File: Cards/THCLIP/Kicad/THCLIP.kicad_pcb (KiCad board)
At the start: 2 copper layers, 47.3 x 35.4 mm, 11 parts, among them J2 Conn_01x03_Pin, J3 Conn_01x05_Pin, U1 RS3K-2424S/H3

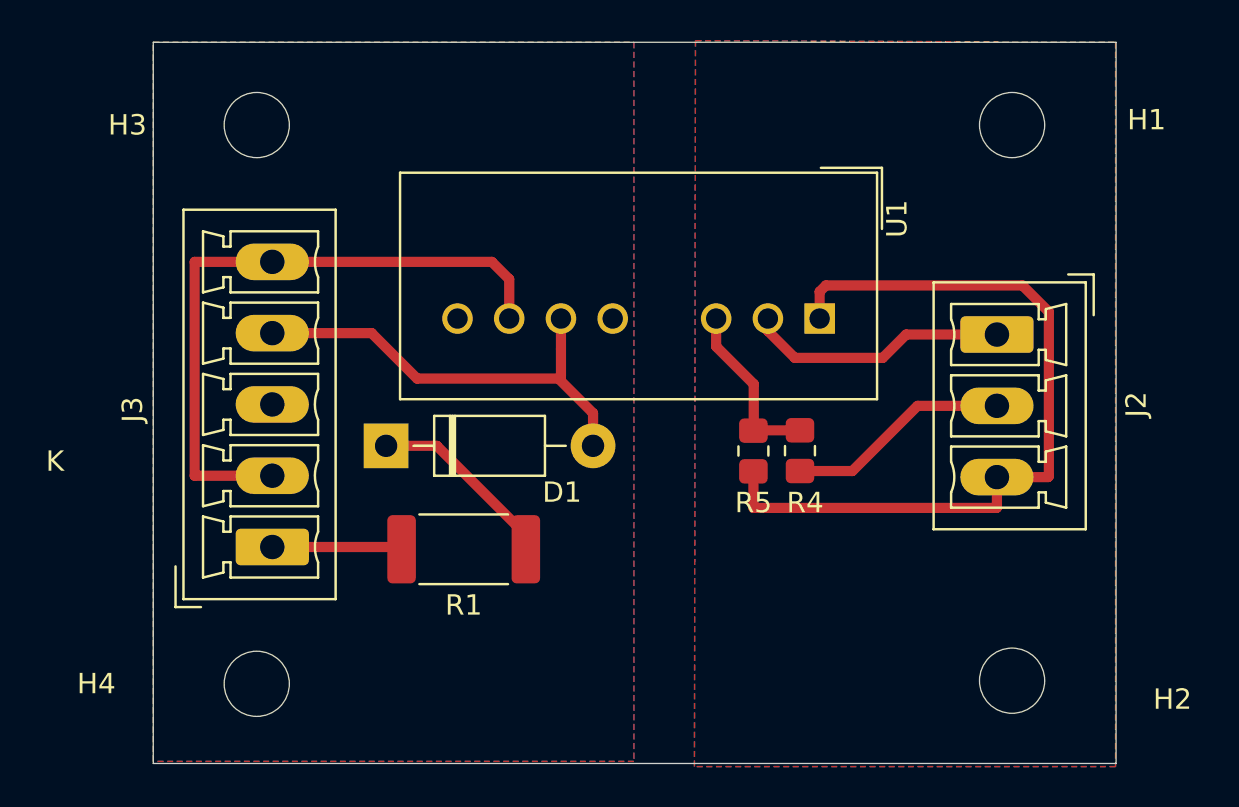
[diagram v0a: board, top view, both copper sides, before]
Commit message: Updated short-circuit resistor to 4k7 for more stable voltage.
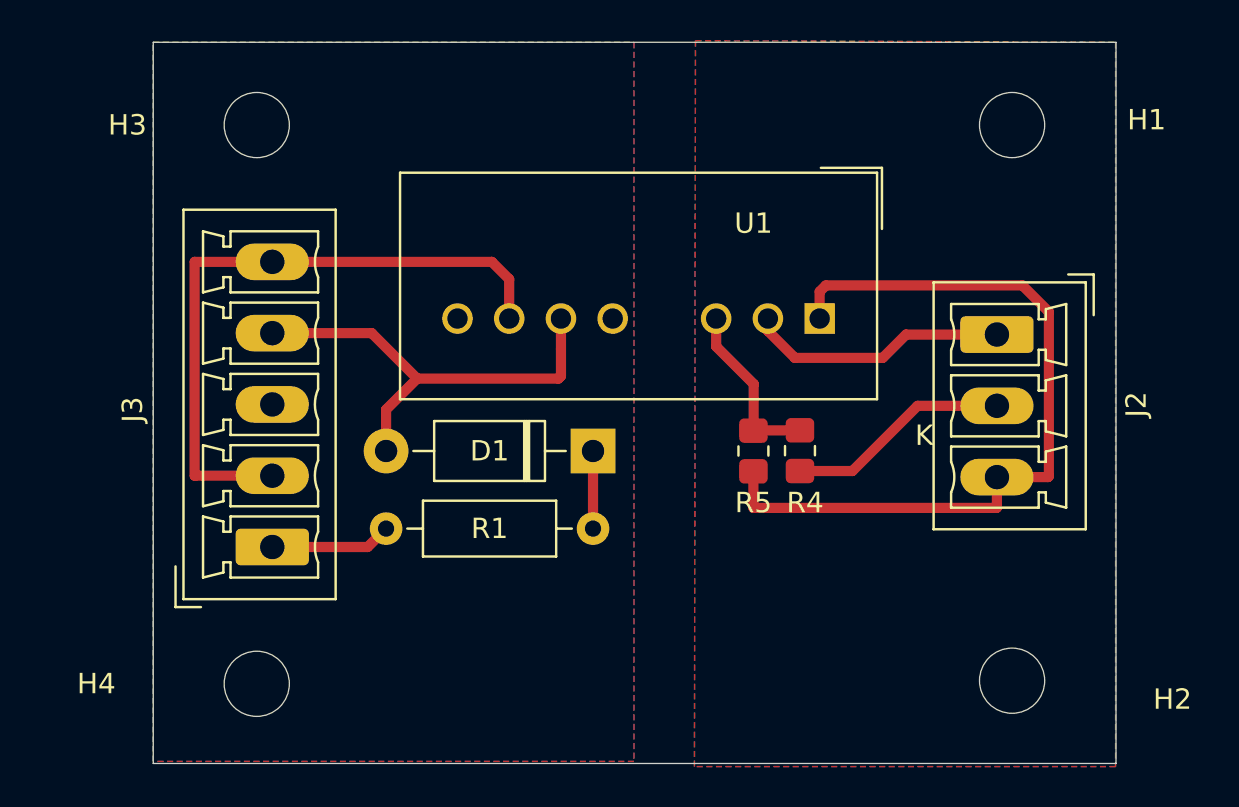
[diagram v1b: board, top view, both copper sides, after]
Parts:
- R1: value 10k -> 4k7; footprint Resistor_SMD:R_2512_6332Metric_Pad1.40x3.35mm_HandSolder -> Resistor_THT:R_Axial_DIN0207_L6.3mm_D2.5mm_P10.16mm_Horizontal
- moved D1 10.2 mm to (174.0, 101.3), turned to 180 degrees
- moved R1 3.94 mm to (163.8, 105.2)
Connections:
- net +24V UNREG renamed 24V UNREG +
- net -24V UNREG renamed 24V UNREG GND
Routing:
- net Net-(D1-K): track 8.67 -> 3.81 mm

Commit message: Updated to read voltage from ground clamp instead of ground in the plasma, which obviously isn't the´real thing.
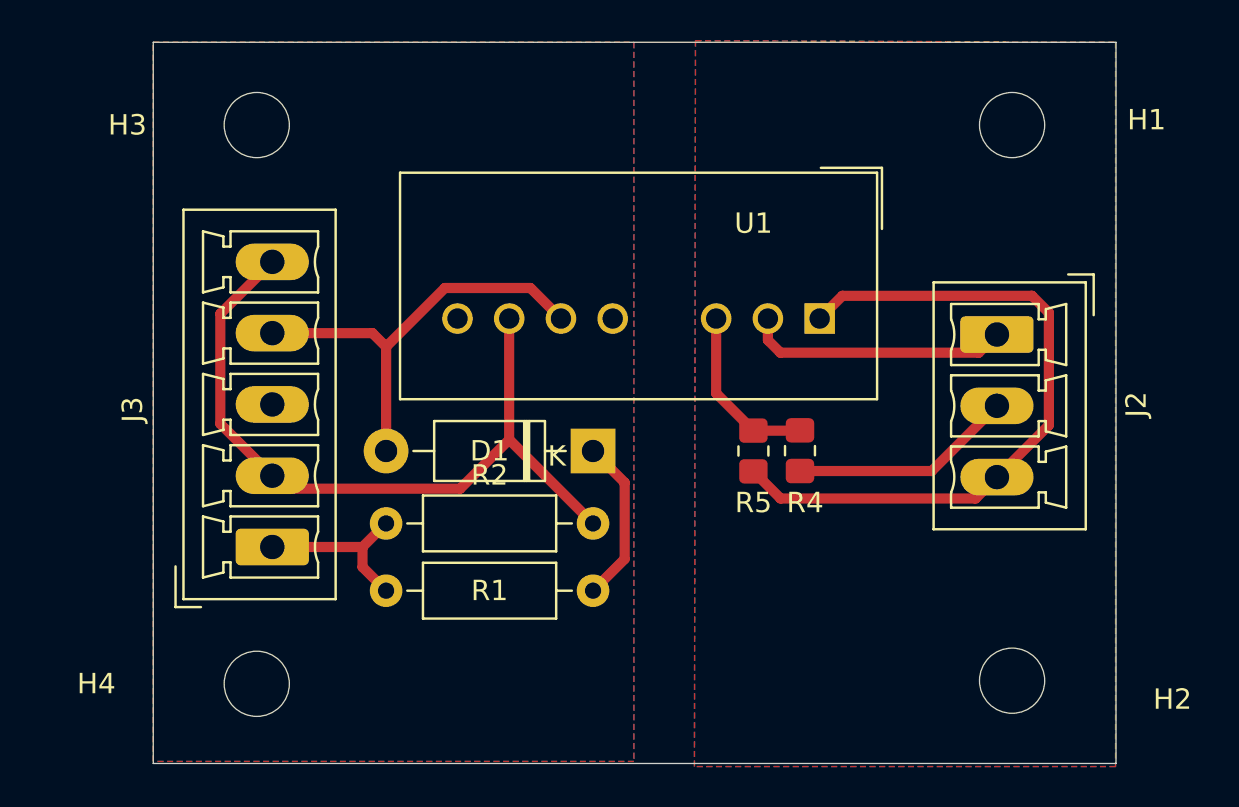
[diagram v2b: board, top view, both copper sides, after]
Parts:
- added R2: 100k, Resistor_THT:R_Axial_DIN0207_L6.3mm_D2.5mm_P10.16mm_Horizontal, F.Cu at (163.8, 104.9)
- R1: value 4k7 -> 2k4
- moved R1 3.05 mm to (163.8, 108.2)
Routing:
- net 24V UNREG GND: track 32.0 -> 37.3 mm
- net -24VDC: track 39.1 -> 34.1 mm
- net Net-(D1-K): track 3.81 -> 8.14 mm
- net WORK PIECE GND (+): track 5.96 -> 8.69 mm
- net 24V UNREG +: track 22.2 -> 21.6 mm
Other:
- board text added: "MetalMusings THCLIP October 2025"
- board text removed: "MetalMusings THCLIP May 2025"
